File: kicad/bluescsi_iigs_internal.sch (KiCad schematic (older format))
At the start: 24 parts, among them J1 Conn_02x13_Odd_Even, J2 Conn_02x13_Odd_Even, J3 105162-0001, J4 Conn_01x02_Male, SW1 SW_SPDT, U1 YAAJ_BluePill, U2 UC560x, UCC56xx, U3 UC560x, UCC56xx, U4 AMS1117-5.0

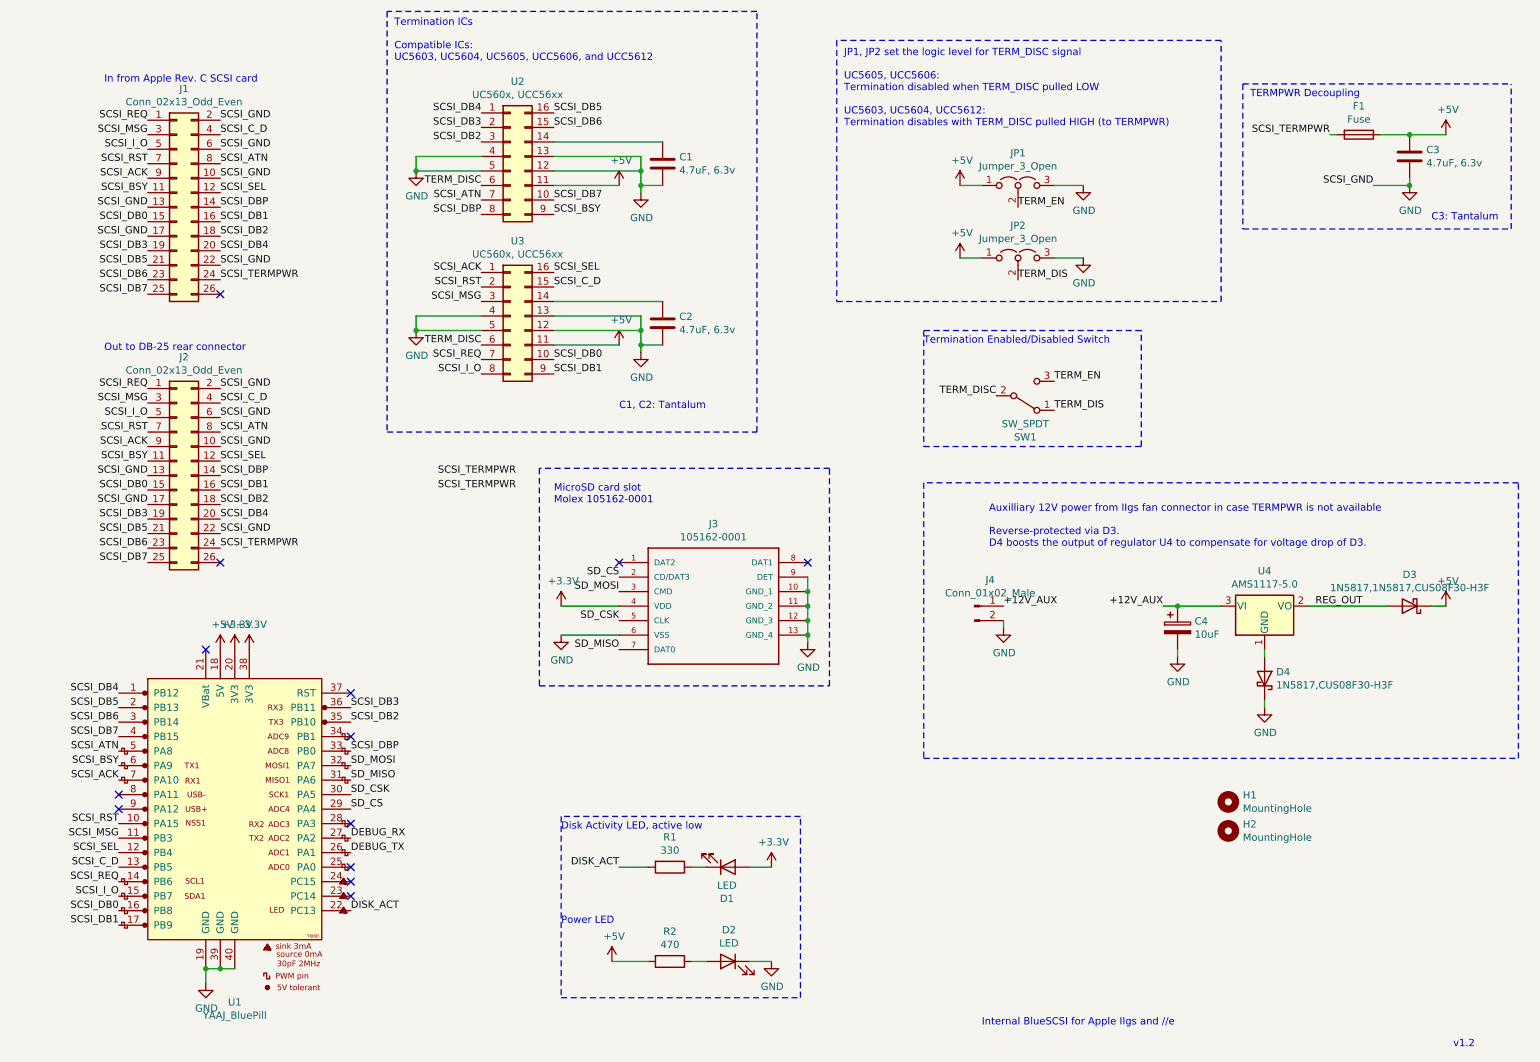
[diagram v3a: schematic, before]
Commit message: Add p-mosfet driver for activity LED
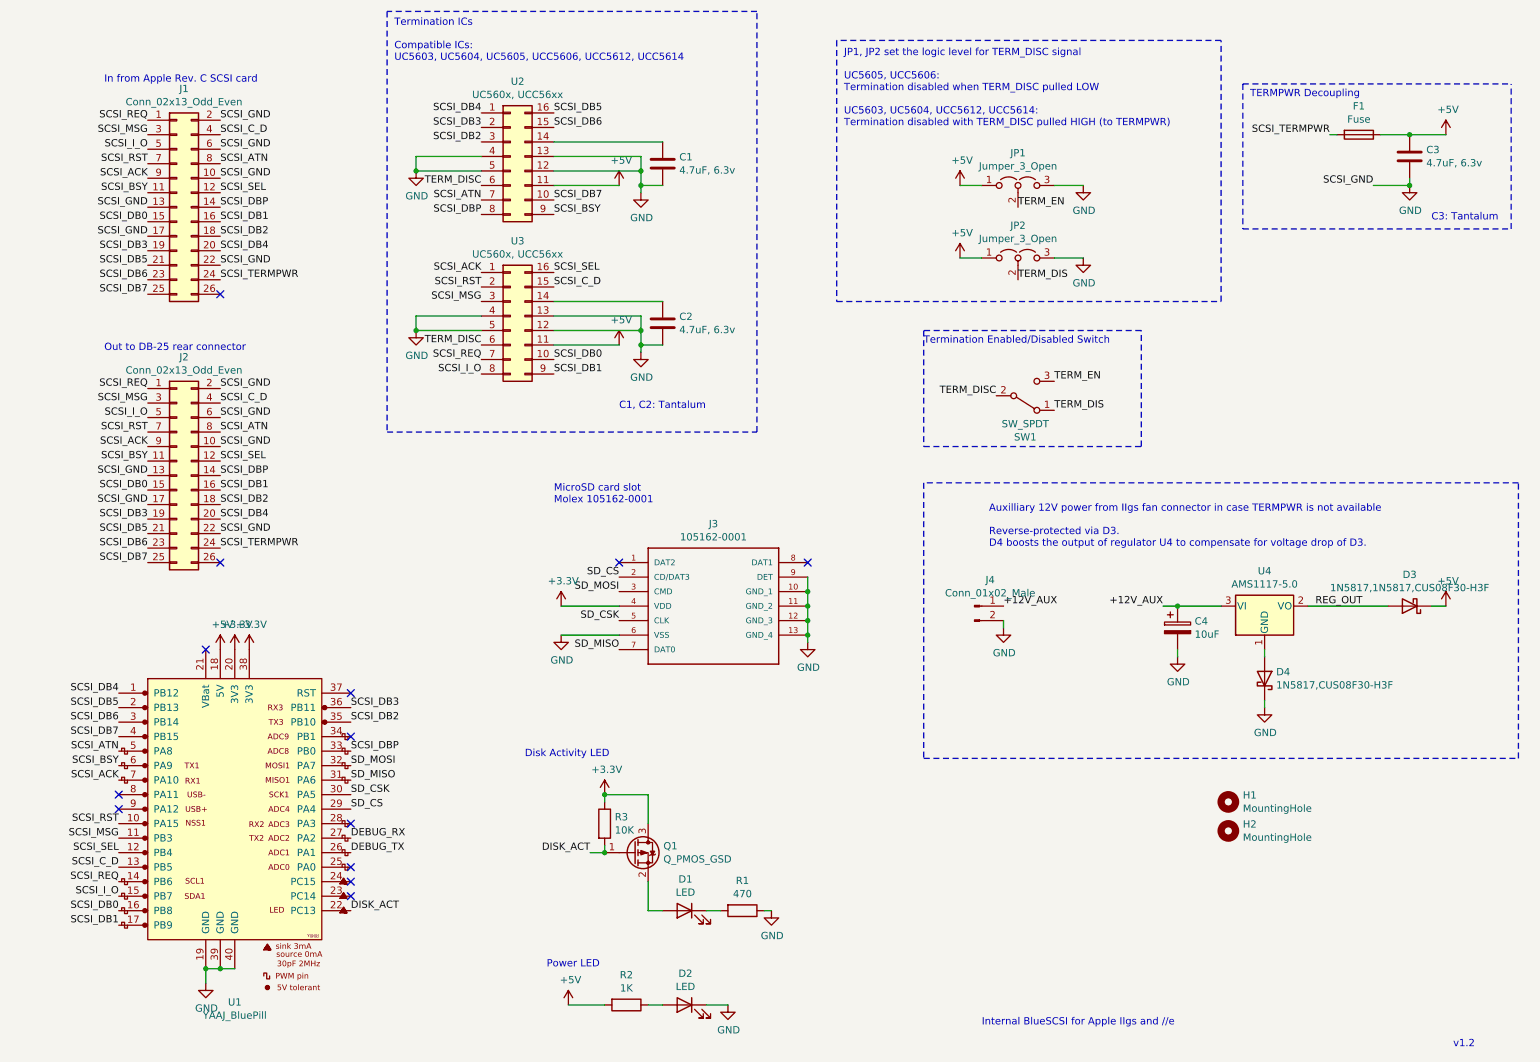
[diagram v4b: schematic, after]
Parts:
- added Q1: Q_PMOS_GSD, Package_TO_SOT_SMD:SOT-23, symbol Device:Q_PMOS_GSD
- added R3: 10K, Resistor_SMD:R_0805_2012Metric_Pad1.20x1.40mm_HandSolder, symbol Device:R
- R1: value 330 -> 470
- R2: value 470 -> 1K
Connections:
- net +3V3: now also Q1.3 (D), R3.1; no longer D1.2 (A)
- net DISK_ACT: now also Q1.1 (G), R3.2; no longer R1.2
- net GND: now also R1.1
- net at D1.1 (K): now also R1.2; no longer R1.1
- new net: D1.2 (A), Q1.2 (S)
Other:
- note added: "Disk Activity LED"
- note added: "JP1, JP2 set the logic level for TERM_DISC signal\n\nUC5605, UCC5606:\nTermination disabled when TERM_DISC pulled LOW\n\nUC5603, UC5604, UCC5612, UCC5614:\nTermination disabled with TERM_DISC pulled HIGH (to TERMPWR)"
- note added: "Termination ICs\n\nCompatible ICs:\nUC5603, UC5604, UC5605, UCC5606, UCC5612, UCC5614"
- note removed: "Disk Activity LED, active low"
- note removed: "JP1, JP2 set the logic level for TERM_DISC signal\n\nUC5605, UCC5606:\nTermination disabled when TERM_DISC pulled LOW\n\nUC5603, UC5604, UCC5612:\nTermination disables with TERM_DISC pulled HIGH (to TERMPWR)"
- note removed: "Termination ICs\n\nCompatible ICs:\nUC5603, UC5604, UC5605, UCC5606, and UCC5612"
- moved on the sheet: D1, D2, R1, R2
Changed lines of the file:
@@
 L Device:LED D2
 U 1 1 60631033
-P 5600 7050
-F 0 "D2" H 5593 7267 50  0000 C CNN
-F 1 "LED" H 5593 7176 50  0000 C CNN
-F 2 "LED_SMD:LED_0805_2012Metric_Pad1.15x1.40mm_HandSolder" H 5600 7050 50  0001 C CNN
-F 3 "~" H 5600 7050 50  0001 C CNN
-	1    5600 7050
+P 5300 7350
+F 0 "D2" H 5293 7567 50  0000 C CNN
+F 1 "LED" H 5293 7476 50  0000 C CNN
+F 2 "LED_SMD:LED_0805_2012Metric_Pad1.15x1.40mm_HandSolder" H 5300 7350 50  0001 C CNN
+F 3 "~" H 5300 7350 50  0001 C CNN
+	1    5300 7350
 	-1   0    0    -1
 $EndComp
@@
 L Device:R R2
 U 1 1 60634BDC
-P 5200 7050
-F 0 "R2" V 4993 7050 50  0000 C CNN
-F 1 "470" V 5084 7050 50  0000 C CNN
-F 2 "Resistor_SMD:R_0805_2012Metric_Pad1.20x1.40mm_HandSolder" V 5130 7050 50  0001 C CNN
-F 3 "~" H 5200 7050 50  0001 C CNN
-	1    5200 7050
+P 4900 7350
+F 0 "R2" V 4693 7350 50  0000 C CNN
+F 1 "1K" V 4784 7350 50  0000 C CNN
+F 2 "Resistor_SMD:R_0805_2012Metric_Pad1.20x1.40mm_HandSolder" V 4830 7350 50  0001 C CNN
+F 3 "~" H 4900 7350 50  0001 C CNN
+	1    4900 7350
 	0    1    1    0
 $EndComp
@@
 L power:GND #PWR0111
 U 1 1 60635DA0
-P 5900 7050
-F 0 "#PWR0111" H 5900 6800 50  0001 C CNN
-F 1 "GND" H 5905 6877 50  0000 C CNN
-F 2 "" H 5900 7050 50  0001 C CNN
-F 3 "" H 5900 7050 50  0001 C CNN
-	1    5900 7050
-	1    0    0    -1
-$EndComp
-Wire Wire Line
-	5750 7050 5900 7050
+P 5600 7350
+F 0 "#PWR0111" H 5600 7100 50  0001 C CNN
+F 1 "GND" H 5605 7177 50  0000 C CNN
+F 2 "" H 5600 7350 50  0001 C CNN
+F 3 "" H 5600 7350 50  0001 C CNN
+	1    5600 7350
+	1    0    0    -1
+$EndComp
+Wire Wire Line
+	5450 7350 5600 7350
 $Comp
 L power:+5V #PWR0113
 U 1 1 60637375
-P 4800 7050
-F 0 "#PWR0113" H 4800 6900 50  0001 C CNN
-F 1 "+5V" H 4815 7223 50  0000 C CNN
-F 2 "" H 4800 7050 50  0001 C CNN
-F 3 "" H 4800 7050 50  0001 C CNN
-	1    4800 7050
-	1    0    0    -1
-$EndComp
-Wire Wire Line
-	5050 7050 4800 7050
+P 4500 7350
+F 0 "#PWR0113" H 4500 7200 50  0001 C CNN
+F 1 "+5V" H 4515 7523 50  0000 C CNN
+F 2 "" H 4500 7350 50  0001 C CNN
+F 3 "" H 4500 7350 50  0001 C CNN
+	1    4500 7350
+	1    0    0    -1
+$EndComp
+Wire Wire Line
+	4750 7350 4500 7350
 $Comp
 L power:GND #PWR0114
@@
 	1    0    0    -1
 $EndComp
-Text Label 3600 3700 0    50   ~ 0
-SCSI_TERMPWR
 Wire Wire Line
 	4400 1500 5000 1500
@@
 	1    0    0    -1
 $EndComp
-Text Label 3600 3800 0    50   ~ 0
-SCSI_TERMPWR
 Wire Wire Line
 	5000 2600 5000 2700
@@
 v1.2
 Text Notes 3300 850  0    50   ~ 0
-Termination ICs\n\nCompatible ICs:\nUC5603, UC5604, UC5605, UCC5606, and UCC5612
+Termination ICs\n\nCompatible ICs:\nUC5603, UC5604, UC5605, UCC5606, UCC5612, UCC5614
 Text Notes 6400 1300 0    50   ~ 0
-JP1, JP2 set the logic level for TERM_DISC signal\n\nUC5605, UCC5606:\nTermination disabled when TERM_DISC pulled LOW\n\nUC5603, UC5604, UCC5612:\nTermination disables with TERM_DISC pulled HIGH (to TERMPWR)
+JP1, JP2 set the logic level for TERM_DISC signal\n\nUC5605, UCC5606:\nTermination disabled when TERM_DISC pulled LOW\n\nUC5603, UC5604, UCC5612, UCC5614:\nTermination disabled with TERM_DISC pulled HIGH (to TERMPWR)
 Text Notes 6950 2800 0    50   ~ 0
 Termination Enabled/Disabled Switch
@@
 DISK_ACT
 Wire Wire Line
-	5350 7050 5450 7050
-Wire Wire Line
-	5350 6400 5450 6400
-Wire Wire Line
-	5750 6400 5900 6400
-Wire Wire Line
-	4850 6400 5050 6400
-Text Label 4850 6400 2    50   ~ 0
+	5050 7350 5150 7350
+Text Label 4650 6300 2    50   ~ 0
 DISK_ACT
-$Comp
-L power:+3.3V #PWR0110
-U 1 1 6062F08F
-P 5900 6400
-F 0 "#PWR0110" H 5900 6250 50  0001 C CNN
-F 1 "+3.3V" H 5915 6573 50  0000 C CNN
-F 2 "" H 5900 6400 50  0001 C CNN
-F 3 "" H 5900 6400 50  0001 C CNN
-	1    5900 6400
-	1    0    0    -1
-$EndComp
 $Comp
 L Device:R R1
 U 1 1 606332E3
-P 5200 6400
-F 0 "R1" V 4993 6400 50  0000 C CNN
-F 1 "330" V 5084 6400 50  0000 C CNN
-F 2 "Resistor_SMD:R_0805_2012Metric_Pad1.20x1.40mm_HandSolder" V 5130 6400 50  0001 C CNN
-F 3 "~" H 5200 6400 50  0001 C CNN
-	1    5200 6400
+P 5700 6700
+F 0 "R1" V 5493 6700 50  0000 C CNN
+F 1 "470" V 5584 6700 50  0000 C CNN
+F 2 "Resistor_SMD:R_0805_2012Metric_Pad1.20x1.40mm_HandSolder" V 5630 6700 50  0001 C CNN
+F 3 "~" H 5700 6700 50  0001 C CNN
+	1    5700 6700
 	0    1    1    0
 $EndComp
@@
 L Device:LED D1
 U 1 1 60632077
-P 5600 6400
-F 0 "D1" H 5593 6617 50  0000 C CNN
-F 1 "LED" H 5593 6526 50  0000 C CNN
-F 2 "LED_SMD:LED_0805_2012Metric_Pad1.15x1.40mm_HandSolder" H 5600 6400 50  0001 C CNN
-F 3 "~" H 5600 6400 50  0001 C CNN
-	1    5600 6400
-	1    0    0    1
-$EndComp
-Text Notes 4450 6150 0    50   ~ 0
-Disk Activity LED, active low
-Wire Notes Line
-	4450 7300 6100 7300
-Wire Notes Line
-	6100 7300 6100 6050
+P 5300 6700
+F 0 "D1" H 5293 6917 50  0000 C CNN
+F 1 "LED" H 5293 6826 50  0000 C CNN
+F 2 "LED_SMD:LED_0805_2012Metric_Pad1.15x1.40mm_HandSolder" H 5300 6700 50  0001 C CNN
+F 3 "~" H 5300 6700 50  0001 C CNN
+	1    5300 6700
+	-1   0    0    -1
+$EndComp
+Text Notes 4200 5650 0    50   ~ 0
+Disk Activity LED
 Wire Notes Line
 	6950 2700 6950 3500
@@
 Text Notes 4400 3900 0    50   ~ 0
 MicroSD card slot\nMolex 105162-0001
-Wire Notes Line
-	4300 3650 4300 5150
-Wire Notes Line
-	4300 5150 6300 5150
-Wire Notes Line
-	6300 5150 6300 3650
-Wire Notes Line
-	6300 3650 4300 3650
-Text Notes 4450 6800 0    50   ~ 0
+Text Notes 4350 7100 0    50   ~ 0
 Power LED
-Wire Notes Line
-	6100 6050 4450 6050
-Wire Notes Line
-	4450 6050 4450 7300
 Wire Notes Line
 	3250 500  3250 3400
@@
 	11000 2000 11000 1000
 $Comp
-L power:+5V #PWR?
+L power:+5V #PWR0110
 U 1 1 609BE96D
 P 4850 2800
-F 0 "#PWR?" H 4850 2650 50  0001 C CNN
+F 0 "#PWR0110" H 4850 2650 50  0001 C CNN
 F 1 "+5V" H 4865 2973 50  0000 C CNN
 F 2 "" H 4850 2800 50  0001 C CNN
@@
 $EndComp
 $Comp
-L power:+5V #PWR?
+L power:+5V #PWR0125
 U 1 1 609BF84F
 P 4850 1700
-F 0 "#PWR?" H 4850 1550 50  0001 C CNN
+F 0 "#PWR0125" H 4850 1550 50  0001 C CNN
 F 1 "+5V" H 4865 1873 50  0000 C CNN
 F 2 "" H 4850 1700 50  0001 C CNN
@@
 Wire Wire Line
 	4400 1700 4850 1700
+$Comp
+L Device:Q_PMOS_GSD Q1
+U 1 1 609D8A80
+P 4950 6300
+F 0 "Q1" H 5155 6346 50  0000 L CNN
+F 1 "Q_PMOS_GSD" H 5155 6255 50  0000 L CNN
+F 2 "Package_TO_SOT_SMD:SOT-23" H 5150 6400 50  0001 C CNN
+F 3 "~" H 4950 6300 50  0001 C CNN
+	1    4950 6300
+	1    0    0    -1
+$EndComp
+$Comp
+L power:+3.3V #PWR0126
+U 1 1 609DCA9E
+P 4750 5900
+F 0 "#PWR0126" H 4750 5750 50  0001 C CNN
+F 1 "+3.3V" H 4765 6073 50  0000 C CNN
+F 2 "" H 4750 5900 50  0001 C CNN
+F 3 "" H 4750 5900 50  0001 C CNN
+	1    4750 5900
+	1    0    0    -1
+$EndComp
+$Comp
+L Device:R R3
+U 1 1 609DE44B
+P 4750 6100
+F 0 "R3" H 4820 6146 50  0000 L CNN
+F 1 "10K" H 4820 6055 50  0000 L CNN
+F 2 "Resistor_SMD:R_0805_2012Metric_Pad1.20x1.40mm_HandSolder" V 4680 6100 50  0001 C CNN
+F 3 "~" H 4750 6100 50  0001 C CNN
+	1    4750 6100
+	1    0    0    -1
+$EndComp
+Wire Wire Line
+	4750 5900 5050 5900
+Wire Wire Line
+	4650 6300 4750 6300
+Wire Wire Line
+	5050 6700 5150 6700
+Wire Wire Line
+	5050 6500 5050 6700
+Wire Wire Line
+	5450 6700 5550 6700
+$Comp
+L power:GND #PWR0127
+U 1 1 609F55CD
+P 5900 6700
+F 0 "#PWR0127" H 5900 6450 50  0001 C CNN
+F 1 "GND" H 5905 6527 50  0000 C CNN
+F 2 "" H 5900 6700 50  0001 C CNN
+F 3 "" H 5900 6700 50  0001 C CNN
+	1    5900 6700
+	1    0    0    -1
+$EndComp
+Wire Wire Line
+	5850 6700 5900 6700
+Wire Wire Line
+	5050 5900 5050 6100
+Wire Wire Line
+	4750 5900 4750 5950
+Connection ~ 4750 5900
+Wire Wire Line
+	4750 6250 4750 6300
+Connection ~ 4750 6300
 $EndSCHEMATC
